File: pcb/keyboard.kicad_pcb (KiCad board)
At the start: 4 copper layers, 146 x 98.8 mm, 63 parts, among them J1 USB4510-03-1-A, J2 Battery, J3 Tag-Connect TC2030, Q1 2N7002, SW1 PWR, SW2 Reset, U1 SRV05-4, U2 BQ24075, U3 BT840, Y1 ECS-.327-9-34B-TR

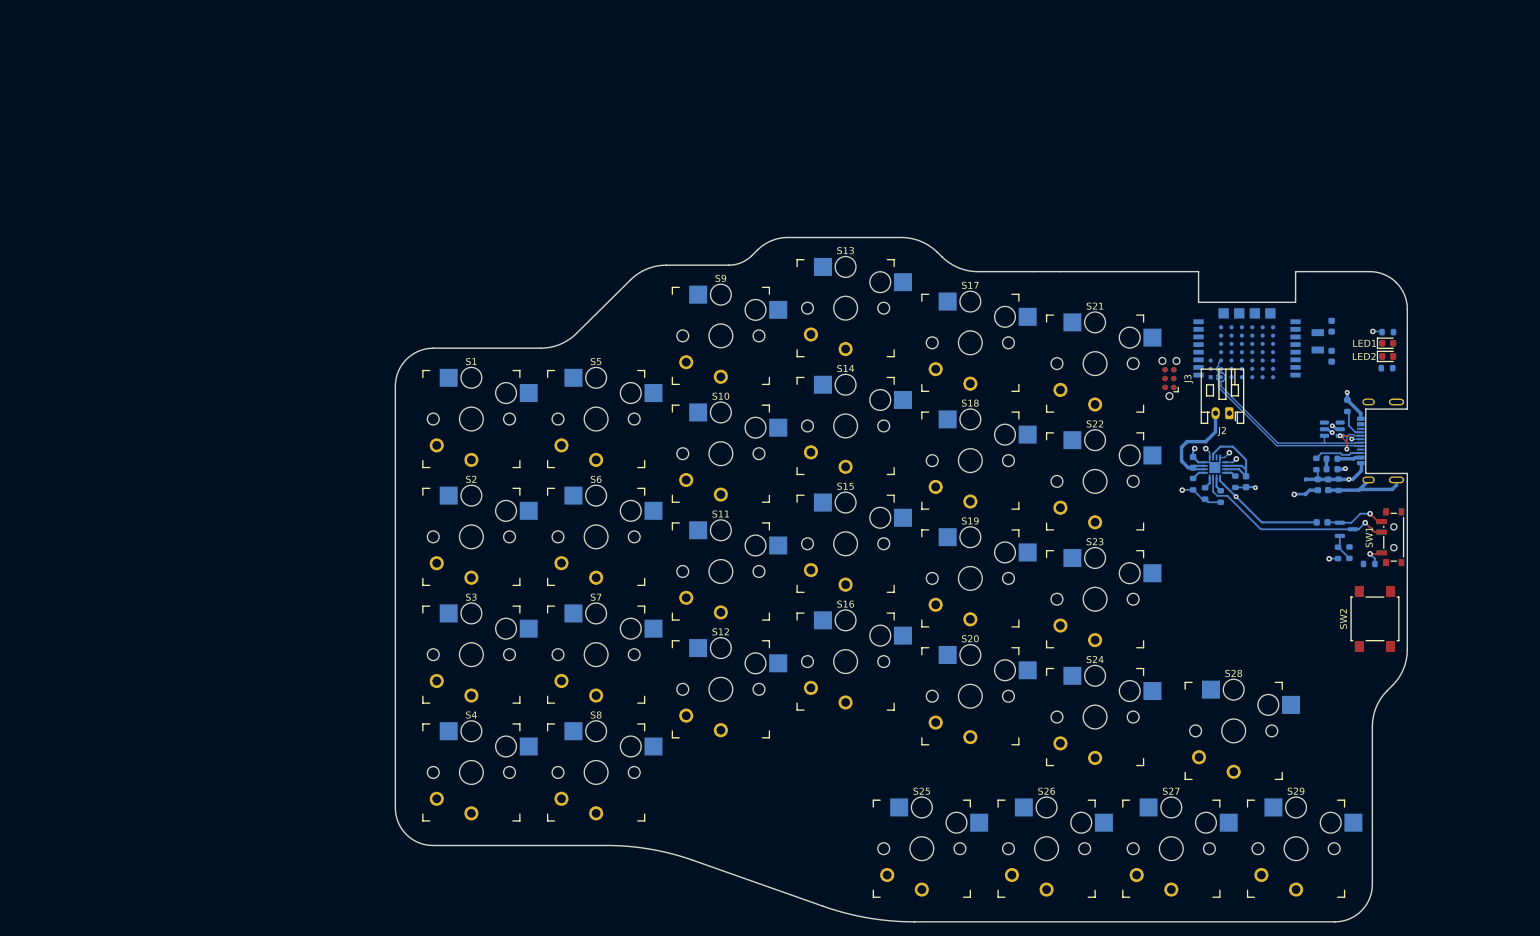
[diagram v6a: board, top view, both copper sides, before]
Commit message: #2 route all the buttons
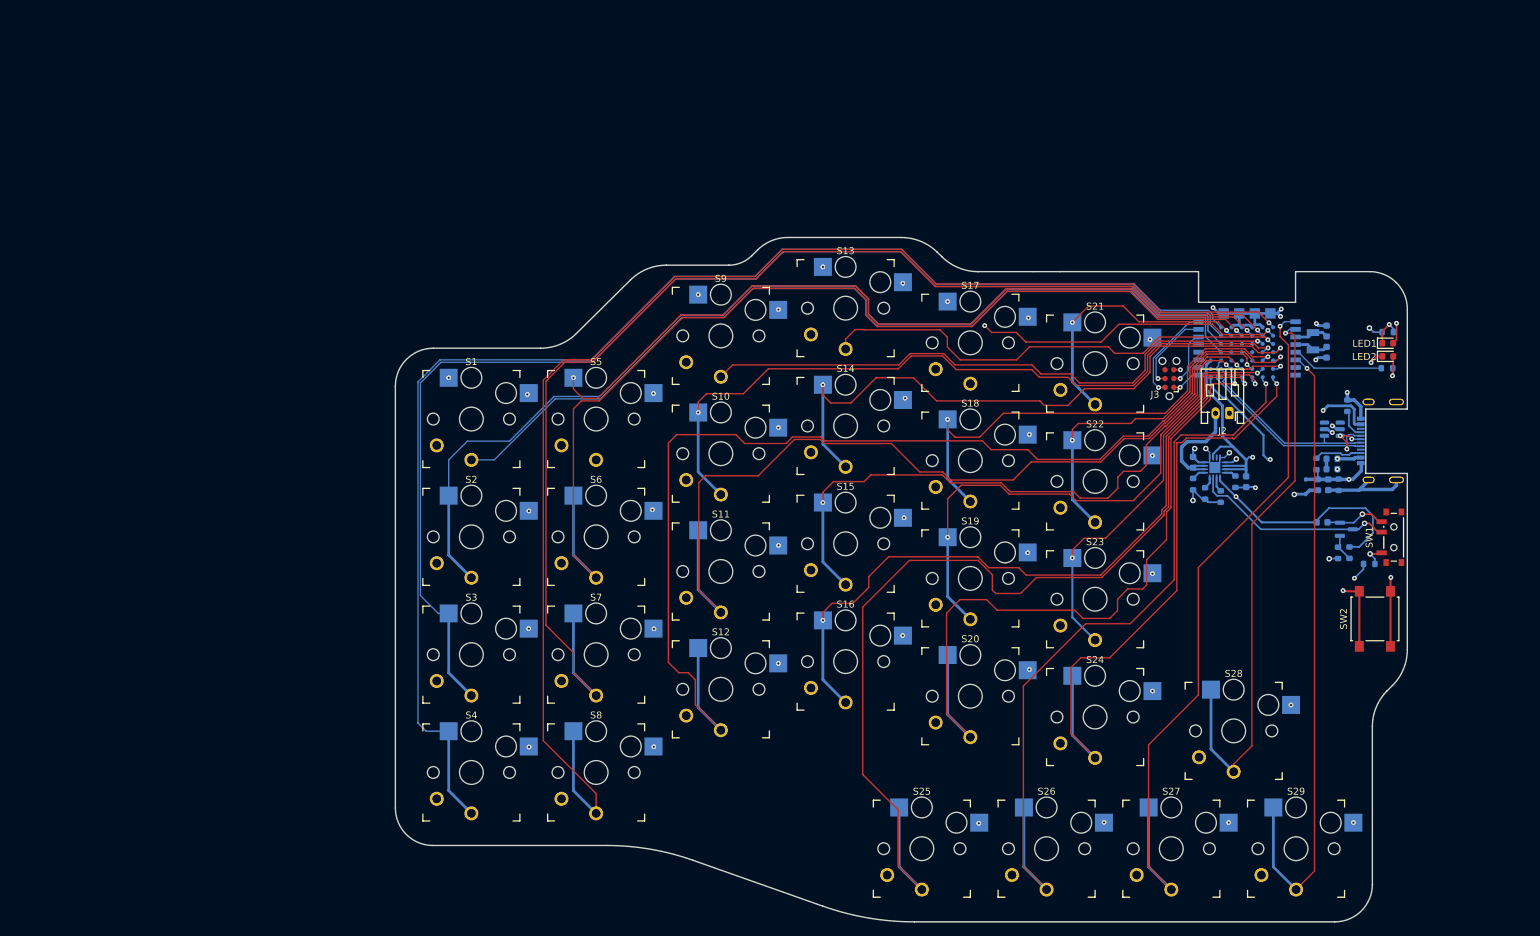
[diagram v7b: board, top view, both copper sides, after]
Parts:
- moved C5 1.00 mm to (267.5, 86.1)
- moved C6 0.93 mm to (267.5, 89.2)
- moved Y1 0.69 mm to (265.6, 87.6)
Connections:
- J3 pad 1: LS-VDD -> VDD
- R12 pad 1: Net-(U3-P0.16) -> Net-(U3-P0.02/AIN0)
- S1 pad 1: P0.26 -> P1.09
- S10 pad 1: P0.29 -> P0.04
- S11 pad 1: P1.10 -> P1.02
- S12 pad 1: P1.08 -> P0.08
- S13 pad 1: P0.28 -> P1.13
- S15 pad 1: P0.07 -> P1.01
- S17 pad 1: P0.24 -> P1.12
- S18 pad 1: P0.04 -> P0.05
- S19 pad 1: P0.08 -> P1.10
- S2 pad 1: P0.27 -> P0.21
- S20 pad 1: P1.04 -> P1.05
- S22 pad 1: P0.20 -> P1.15
- S23 pad 1: P1.02 -> P0.07
- S24 pad 1: P1.05 -> P1.06
- S25 pad 1: P0.12 -> P1.04
- S26 pad 1: P0.25 -> P1.08
- S27 pad 1: P1.07 -> P0.26
- S28 pad 1: P0.21 -> P0.27
- S29 pad 1: P0.21 -> P0.03
- S3 pad 1: unconnected-(S3-Pad1) -> P0.20
- S4 pad 1: unconnected-(S4-Pad1) -> P1.07
- S5 pad 1: P1.11 -> P0.25
- S6 pad 1: P1.12 -> P0.24
- S7 pad 1: P0.05 -> P0.28
- S8 pad 1: P1.06 -> P1.11
- S9 pad 1: P1.13 -> P0.29
- U3 pad 5: unconnected-(U3-P0.02/AIN0-Pad5) -> Net-(U3-P0.02/AIN0)
- U3 pad 6: unconnected-(U3-P0.03/AIN1-Pad6) -> P0.03
- U3 pad 9: unconnected-(U3-VDD-Pad9) -> VDD
- U3 pad D3: Net-(U3-P0.16) -> unconnected-(U3-P0.16-PadD3)
- U3 pad E6: P0.12 -> unconnected-(U3-P0.12-PadE6)
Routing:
- net P1.11: track 0.00 -> 196.7 mm, vias 0 -> 1
- net P1.07: track 0.00 -> 196.2 mm
- net P0.20: track 0.00 -> 178.2 mm
- net P0.28: track 0.00 -> 177.8 mm, vias 0 -> 1
- net P0.08: track 0.00 -> 155.4 mm, vias 0 -> 1
- net P0.24: track 0.00 -> 151.0 mm, vias 0 -> 1
- net P0.21: track 0.00 -> 150.3 mm
- net P1.09: track 0.00 -> 142.5 mm, vias 0 -> 1
- net P1.04: track 0.00 -> 141.1 mm, vias 0 -> 1
- net P0.25: track 0.00 -> 128.6 mm, vias 0 -> 2
- net P1.02: track 0.00 -> 126.7 mm, vias 0 -> 1
- net P1.08: track 0.00 -> 111.4 mm, vias 0 -> 1
- net P0.26: track 0.00 -> 107.2 mm, vias 0 -> 1
- net P0.04: track 0.00 -> 106.6 mm, vias 0 -> 2
- net P1.03: track 0.00 -> 103.9 mm, vias 0 -> 2
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
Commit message: #2 Add mounting holes
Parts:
- added H1: MountingHole, MountingHole:MountingHole_2.2mm_M2, F.Cu at (186.1, 153.9)
- added H2: MountingHole, MountingHole:MountingHole_2.2mm_M2, F.Cu at (168.5, 87.2)
- added H3: MountingHole, MountingHole:MountingHole_2.2mm_M2, F.Cu at (267.6, 146.6)
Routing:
- net P0.24: track 151.0 -> 152.5 mm
- net P0.25: track 128.6 -> 129.9 mm
- net P1.09: track 142.5 -> 143.7 mm
- net P0.21: track 150.3 -> 151.4 mm
